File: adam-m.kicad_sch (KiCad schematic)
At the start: 21 parts, among them J1 AudioJack4dpb, SW1 SW_Push, SW10 SW_Push, SW11 SW_Push, SW12 SW_Push, SW13 SW_Push, SW14 SW_Push, SW15 SW_Push, SW16 SW_Push, SW17 SW_Push, SW2 SW_Push, SW3 SW_Push, SW4 SW_Push, SW5 SW_Push, SW6 SW_Push, SW7 SW_Push, SW8 SW_Push, SW9 SW_Push, U1 ProMicro-kbd

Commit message: update
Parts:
- U1: value ProMicro-kbd -> ProMicro-pinout
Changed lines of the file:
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@@
       (effects (font (size 1.524 1.524)))
     )
-    (property "Value" "ProMicro-kbd" (at 195.58 47.3202 0)
+    (property "Value" "ProMicro-pinout" (at 195.58 47.3202 0)
       (effects (font (size 1.524 1.524)))
     )

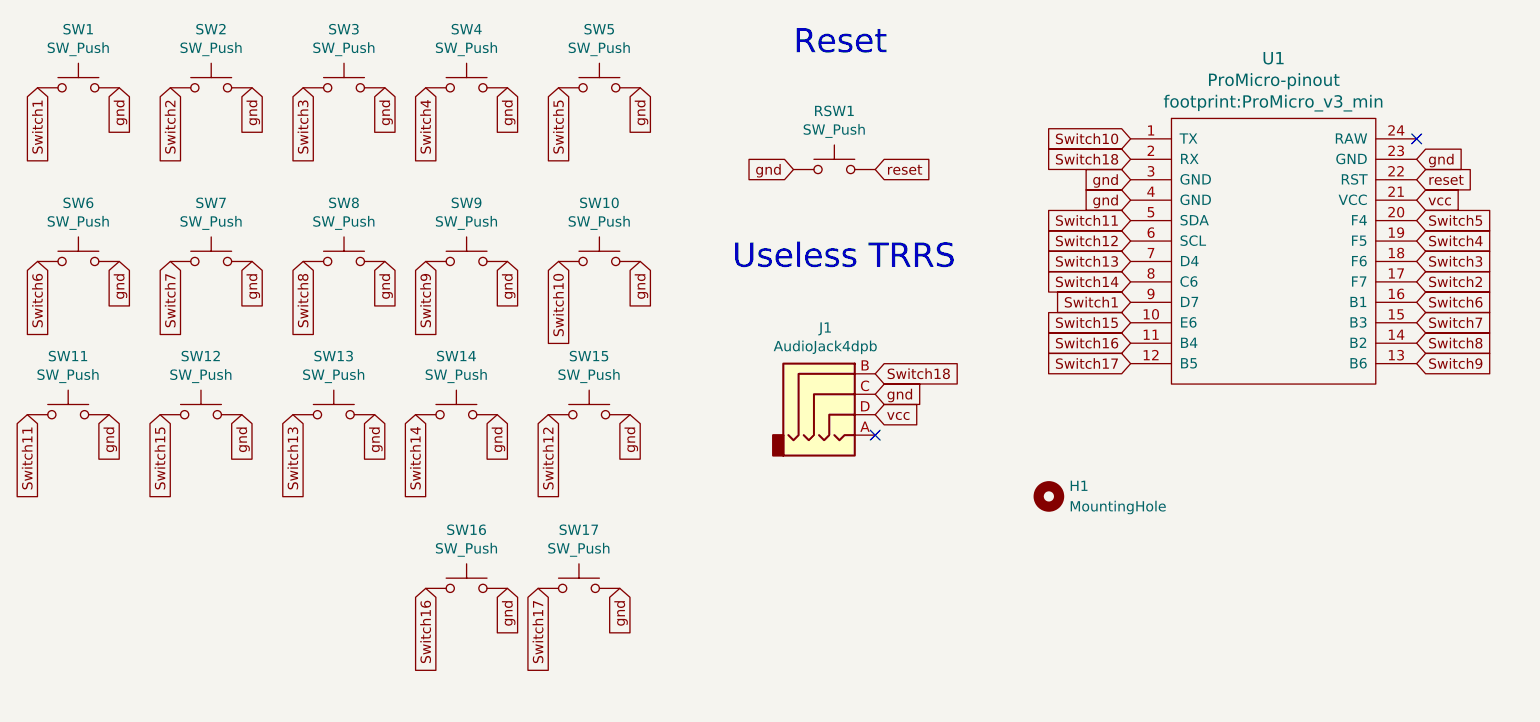
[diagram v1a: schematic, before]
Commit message: rework switch numbering, rearrange schematic for clarity
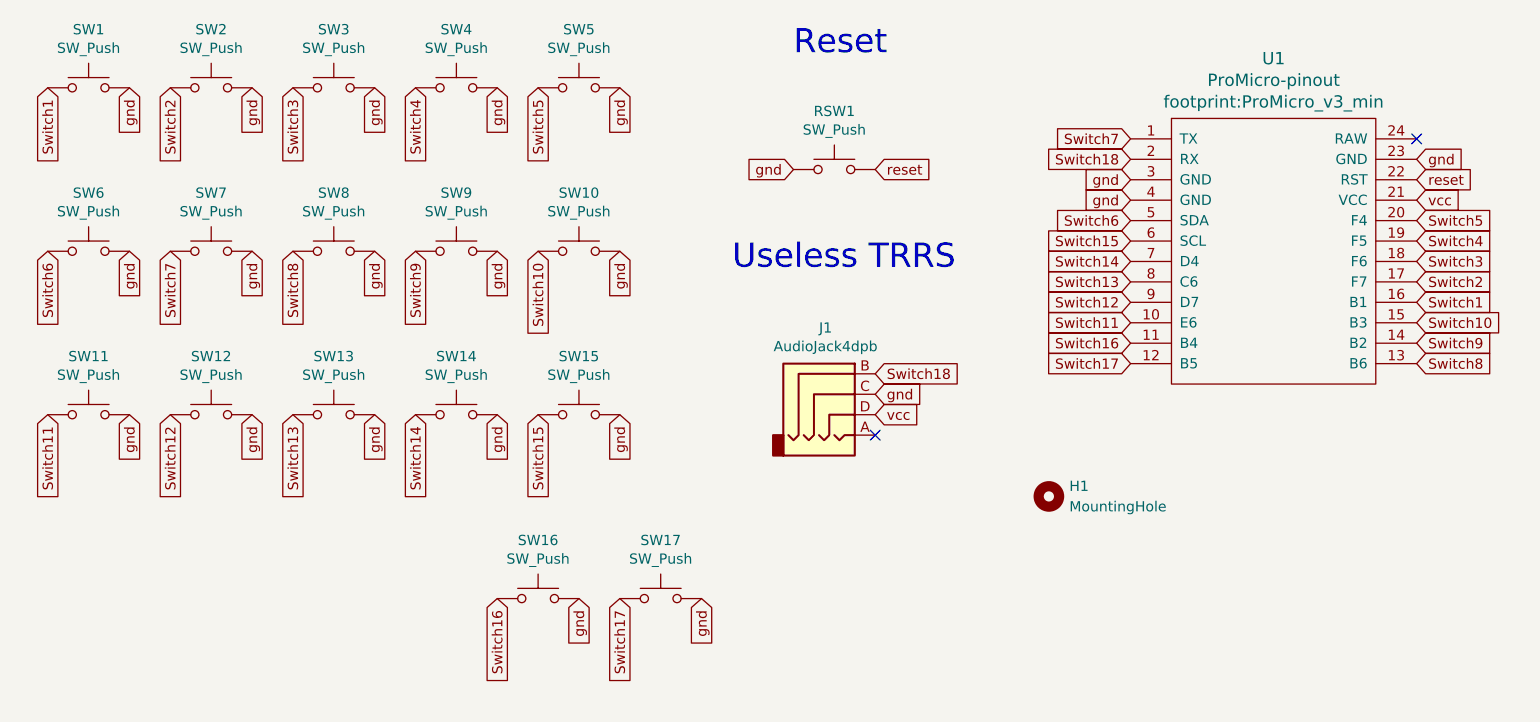
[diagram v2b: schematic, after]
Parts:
- renumbered SW6 to SW1, SW7 to SW10, SW12 to SW11, SW1 to SW12, SW14 to SW13, SW13 to SW14, SW11 to SW6, SW10 to SW7, SW9 to SW8, SW8 to SW9
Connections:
- net Switch1: now also SW1.1, U1.16 (B1); no longer SW12.1, U1.9 (D7)
- net Switch10: now also SW10.1, U1.15 (B3); no longer SW7.1, U1.1 (TX)
- net Switch11: now also SW11.1, U1.10 (E6); no longer SW6.1, U1.5 (SDA)
- net Switch12: now also SW12.1, U1.9 (D7); no longer SW15.1, U1.6 (SCL)
- net Switch13: now also SW13.1, U1.8 (C6); no longer SW14.1, U1.7 (D4)
- net Switch14: now also SW14.1, U1.7 (D4); no longer SW13.1, U1.8 (C6)
- net Switch15: now also SW15.1, U1.6 (SCL); no longer SW11.1, U1.10 (E6)
- net Switch6: now also SW6.1, U1.5 (SDA); no longer SW1.1, U1.16 (B1)
- net Switch7: now also SW7.1, U1.1 (TX); no longer SW10.1, U1.15 (B3)
- net Switch8: now also SW8.1, U1.13 (B6); no longer SW9.1, U1.14 (B2)
- net Switch9: now also SW9.1, U1.14 (B2); no longer SW8.1, U1.13 (B6)
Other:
- moved on the sheet: SW1, SW10, SW11, SW12, SW13, SW14, SW15, SW16, SW17, SW3, SW4, SW5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

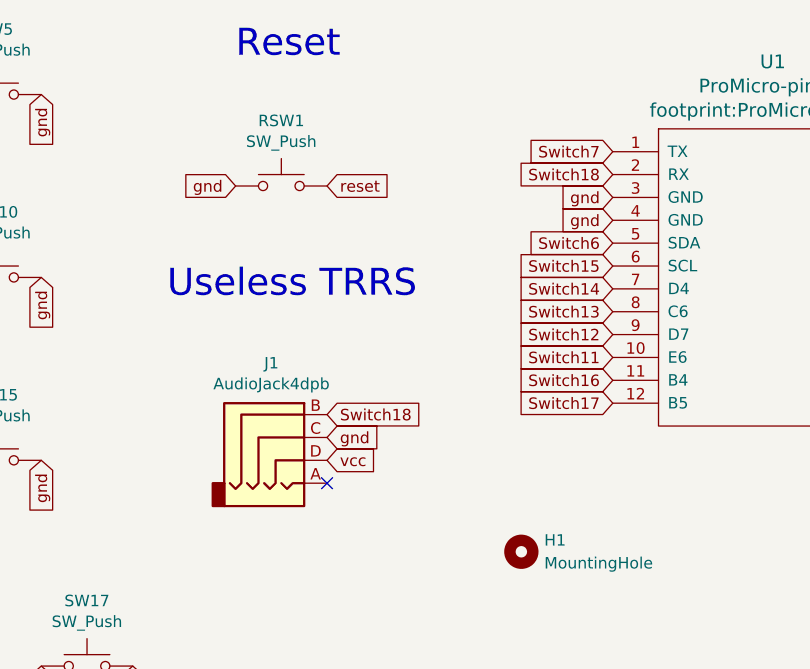
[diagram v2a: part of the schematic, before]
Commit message: Re-assign TRRS pad labels
This is a hacked symbol anyway, may as well make it a logical one. Now
the pad order flows from one end to another of the internal
connections (note that sleeve connection is at opposite end to pin so
*appears* out-of-order on PCB footprint). Also explicitly include pads
that are shorted together by reversible footprint and reflect this in
schematic.
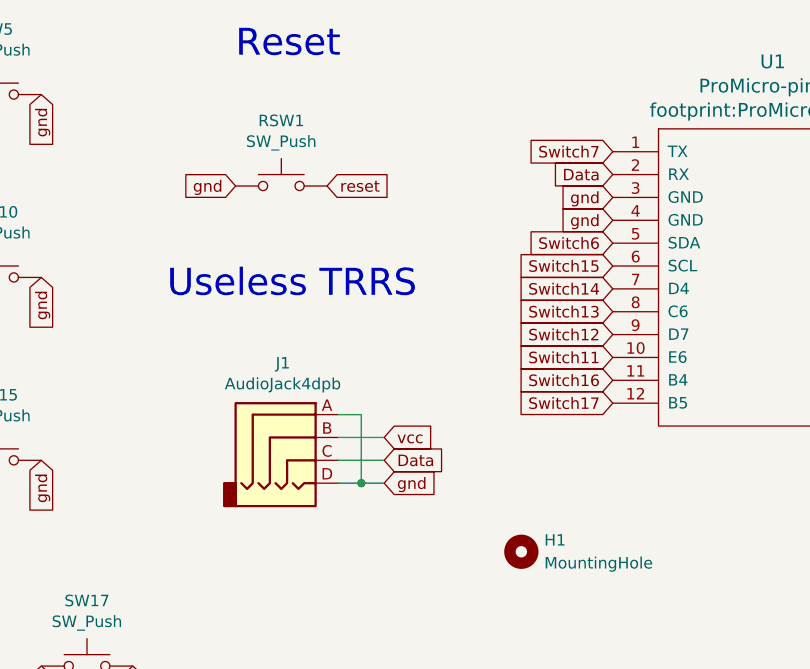
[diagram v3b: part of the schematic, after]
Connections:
- net gnd: now also J1.A, J1.D; no longer J1.C
- net vcc: now also J1.B; no longer J1.D
- net Switch18 renamed Data
- net Data: now also J1.C; no longer J1.B
- no-connect marks 2 -> 1
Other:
- moved on the sheet: J1
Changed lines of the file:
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@@
 (kicad_sch (version 20230121) (generator eeschema)
   (paper "A4")
-  (no_connect (at 146.05 91.44))
+  (junction (at 149.86 91.44) (diameter 0) (color 0 0 0 0)
+  )
   (no_connect (at 213.36 54.61))
+  (wire (pts (xy 149.86 91.44) (xy 152.4 91.44))
+    (stroke (width 0) (type default))
+  )
+  (wire (pts (xy 147.32 88.9) (xy 152.4 88.9))
+    (stroke (width 0) (type default))
+  )
+  (wire (pts (xy 147.32 91.44) (xy 149.86 91.44))
+    (stroke (width 0) (type default))
+  )
+  (wire (pts (xy 149.86 83.82) (xy 149.86 91.44))
+    (stroke (width 0) (type default))
+  )
+  (wire (pts (xy 147.32 83.82) (xy 149.86 83.82))
+    (stroke (width 0) (type default))
+  )
+  (wire (pts (xy 147.32 86.36) (xy 152.4 86.36))
+    (stroke (width 0) (type default))
+  )
   (text "Useless TRRS\n" (at 128.27 71.12 0)
     (effects (font (size 2.9972 2.9972)) (justify left bottom))
@@
     )
   )
-  (global_label "Switch18" (shape input) (at 146.05 83.82 0)
-    (effects (font (size 1.27 1.27)) (justify left))
-    (property "Intersheetrefs" "${INTERSHEET_REFS}" (at 146.05 83.82 0)
+  (global_label "Data" (shape input) (at 152.4 88.9 0)
+    (effects (font (size 1.27 1.27)) (justify left))
+    (property "Intersheetrefs" "${INTERSHEET_REFS}" (at 152.4 88.9 0)
       (effects (font (size 1.27 1.27)) hide)
     )
@@
     )
   )
-  (global_label "Switch18" (shape input) (at 177.8 57.15 180)
+  (global_label "Data" (shape input) (at 177.8 57.15 180)
     (effects (font (size 1.27 1.27)) (justify right))
     (property "Intersheetrefs" "${INTERSHEET_REFS}" (at 177.8 57.15 0)
@@
     )
   )
-  (global_label "vcc" (shape input) (at 146.05 88.9 0)
-    (effects (font (size 1.27 1.27)) (justify left))
-    (property "Intersheetrefs" "${INTERSHEET_REFS}" (at 146.05 88.9 0)
+  (global_label "vcc" (shape input) (at 152.4 86.36 0)
+    (effects (font (size 1.27 1.27)) (justify left))
+    (property "Intersheetrefs" "${INTERSHEET_REFS}" (at 152.4 86.36 0)
       (effects (font (size 1.27 1.27)) hide)
     )
@@
     )
   )
-  (global_label "gnd" (shape input) (at 146.05 86.36 0)
-    (effects (font (size 1.27 1.27)) (justify left))
-    (property "Intersheetrefs" "${INTERSHEET_REFS}" (at 146.05 86.36 0)
+  (global_label "gnd" (shape input) (at 152.4 91.44 0)
+    (effects (font (size 1.27 1.27)) (justify left))
+    (property "Intersheetrefs" "${INTERSHEET_REFS}" (at 152.4 91.44 0)
       (effects (font (size 1.27 1.27)) hide)
     )
@@
     )
   )
-  (symbol (lib_id "sweep-high-rescue:AudioJack4dpb-tokas_bp") (at 140.97 86.36 0) (unit 1)
-    (in_bom yes) (on_board yes) (dnp no)
-    (property "Reference" "J1" (at 139.8778 78.105 0)
-      (effects (font (size 1.27 1.27)))
-    )
-    (property "Value" "AudioJack4dpb" (at 139.8778 80.4164 0)
-      (effects (font (size 1.27 1.27)))
-    )
-    (property "Footprint" "footprint:TRRS-PJ-DPB2" (at 140.97 86.36 0)
-      (effects (font (size 1.27 1.27)) hide)
-    )
-    (property "Datasheet" "~" (at 140.97 86.36 0)
-      (effects (font (size 1.27 1.27)) hide)
-    )
+  (symbol (lib_id "sweep-high-rescue:AudioJack4dpb-tokas_bp") (at 142.24 86.36 0) (unit 1)
+    (in_bom yes) (on_board yes) (dnp no)
+    (property "Reference" "J1" (at 141.1478 78.105 0)
+      (effects (font (size 1.27 1.27)))
+    )
+    (property "Value" "AudioJack4dpb" (at 141.1478 80.4164 0)
+      (effects (font (size 1.27 1.27)))
+    )
+    (property "Footprint" "footprint:TRRS-PJ-DPB2" (at 142.24 86.36 0)
+      (effects (font (size 1.27 1.27)) hide)
+    )
+    (property "Datasheet" "~" (at 142.24 86.36 0)
+      (effects (font (size 1.27 1.27)) hide)
+    )
+    (pin "D")
     (pin "A")
     (pin "B")
     (pin "C")
-    (pin "D")
-    (instances
-      (project "adam-m"
+    (instances
+      (project "adam-m"
